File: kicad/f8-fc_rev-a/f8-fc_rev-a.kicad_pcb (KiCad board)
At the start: 4 copper layers, 34.7 x 34.7 mm, 114 parts, among them J1 Battery, J10 USART1, J11 USART2, J12 FC-ESC con, J13 Motors2, J14 UART4, J15 USART6, J16 I2C, J17 I2C, J18 I2C, J19 Debug, J2 M1, J3 M2, J4 M3, J5 M4, J6 M5, J7 M6, J8 M7, J9 M8, Q1 PMOS, Q2 2300A, Q3 2300A, Q4 2300A, Q5 2300A, Q6 2300A, Q7 2300A, Q8 2300A, Q9 2300A, SW1 SW_SPST, U1 STM32F405RGT6, U13 W25Q128JVS, U14 INA180A3, U2 BMP388, U3 BMI270, U4 TPS62172DSG, U5 GT-USB-7010AN, Y1 8 MHz

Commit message: Added some silkscreen
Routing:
- net VBAT: track 27.7 -> 37.5 mm
- net TX2: track 11.4 -> 17.3 mm
- net RX2: vias 3 -> 2
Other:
- board text removed: "rev. A"

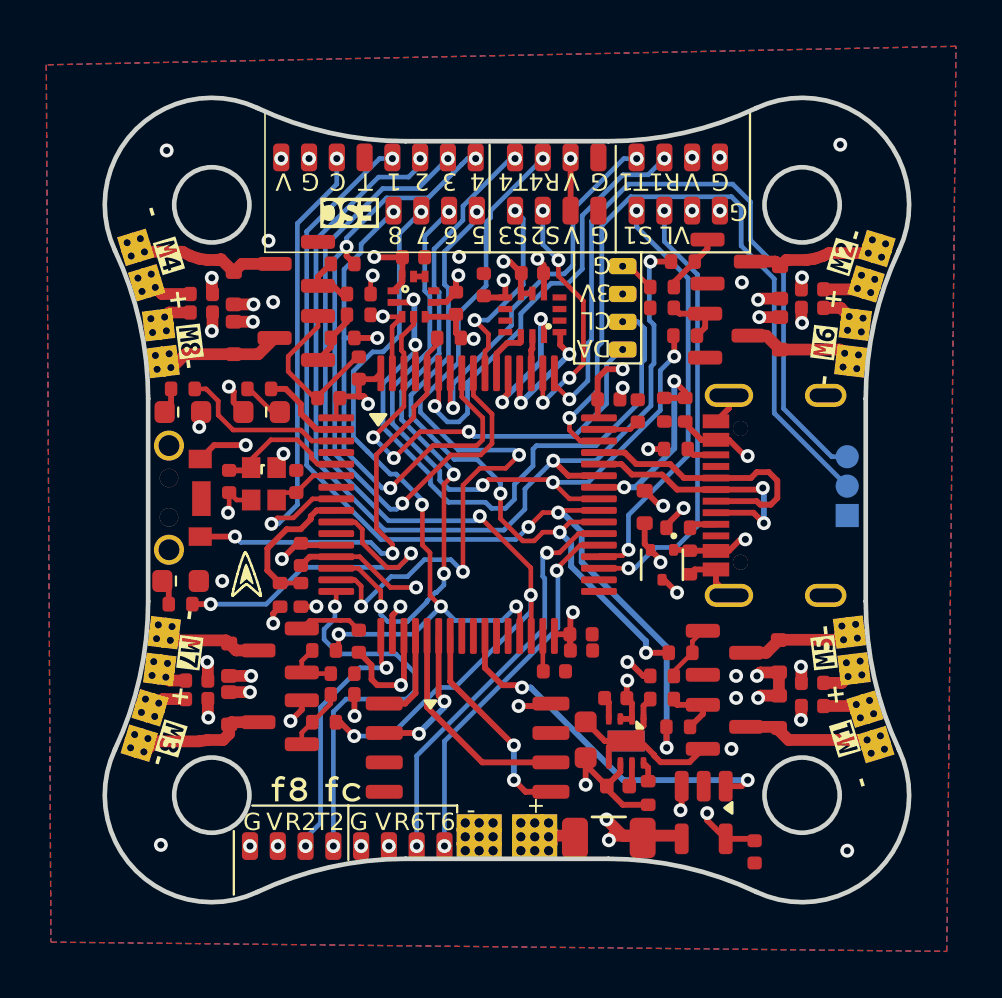
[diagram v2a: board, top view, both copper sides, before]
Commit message: Clenaup: Almost ready for order
Need to get the 30.5x30.5 holes into the outline as well, otherwise all looks good
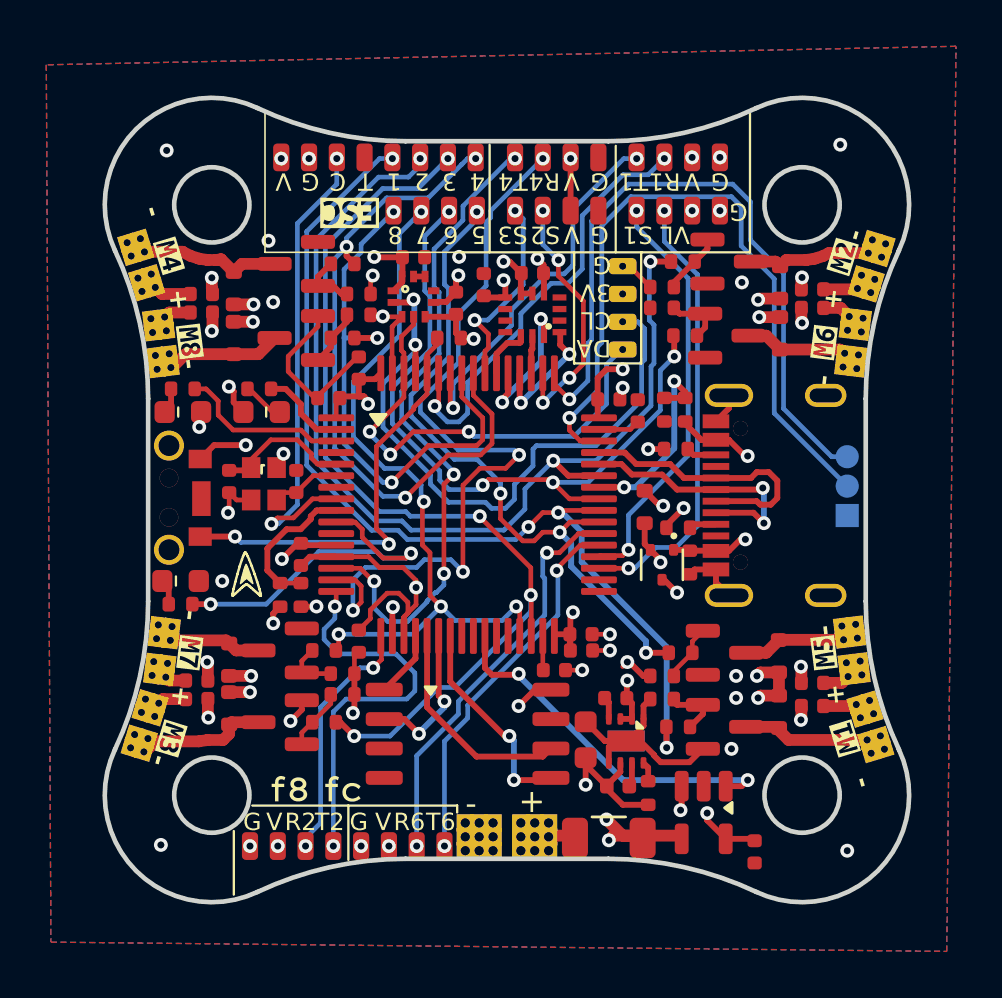
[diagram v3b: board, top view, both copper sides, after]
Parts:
- moved U13 0.60 mm to (166.4, 132.9)
- turned C12 to -90 degrees
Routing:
- net +3.3V: track 109.0 -> 111.3 mm, vias 13 -> 12
- net GND: track 57.1 -> 58.7 mm, vias 42 -> 45
- net RX4: track 32.4 -> 33.9 mm
- net FLASH_CS: track 4.01 -> 2.88 mm
- net BOOT0: track 19.3 -> 18.5 mm
- net M4: track 29.7 -> 29.2 mm
- net RX2: track 11.3 -> 10.8 mm

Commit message: rev. A is ready to order!
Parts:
- moved R2 0.46 mm to (175.9, 119.3)
- moved R3 0.45 mm to (174.9, 119.3)
- moved C19 0.27 mm to (154.8, 131.6)
- moved C20 0.18 mm to (154.9, 113.7)
- moved C23 0.15 mm to (154.8, 130.6)
- moved R10 0.12 mm to (175.5, 123.9)
- moved C5 0.11 mm to (164.1, 112.4)
- moved D11 0.10 mm to (156.2, 129.7)
- moved D4 0.10 mm to (174.1, 123.2)
- moved R9 0.10 mm to (175.4, 120.7)
- moved D7 0.10 mm to (156.2, 131.8)
- moved D2 0.09 mm to (154.1, 119.1)
- moved R5 0.09 mm to (154.0, 118.0)
- moved C16 0.05 mm to (159.2, 125.1)
- moved R18 0.05 mm to (160.2, 132.4)
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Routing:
- net GND: track 58.7 -> 62.5 mm, vias 45 -> 53
- net +3.3V: track 111.3 -> 108.7 mm
- net VBUS: track 16.1 -> 15.1 mm
- net USB+: track 12.0 -> 11.2 mm
- net USB-: track 11.4 -> 10.8 mm
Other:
- board size 34.7 x 34.7 mm -> 35.5 x 35.5 mm
- board text added: "GND"
- board text added: "SCK"
- board text added: "SWD"

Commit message: Updated cap to 0603 (C2) and driver caps from 10uf to 1uf. This is because these needs to tolerate higher voltages than 10V and that isn't available at 0402 10uF..
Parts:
- C17, C18, C19, C20, C21, C22, C23, C24: value 10uF -> 1uF
- C2: footprint custom:C_0402_1005Metric_NoSilk -> custom:C_0603_1608Metric_NoSilk
- moved C2 0.39 mm to (172.5, 131.2)
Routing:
- net VSYS: track 10.2 -> 11.5 mm
